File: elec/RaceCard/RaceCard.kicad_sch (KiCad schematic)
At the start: 8 parts

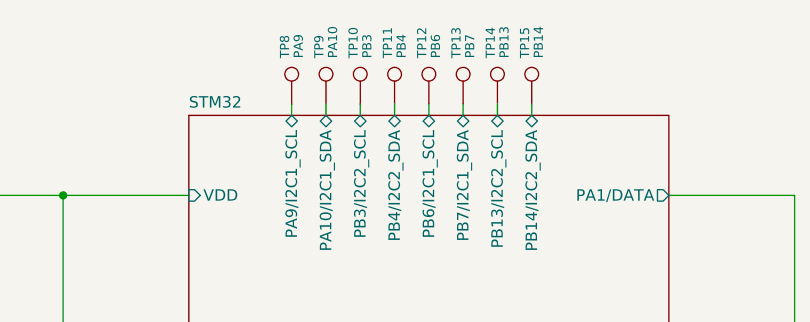
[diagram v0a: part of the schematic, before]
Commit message: Fix des footprints et edge cuts
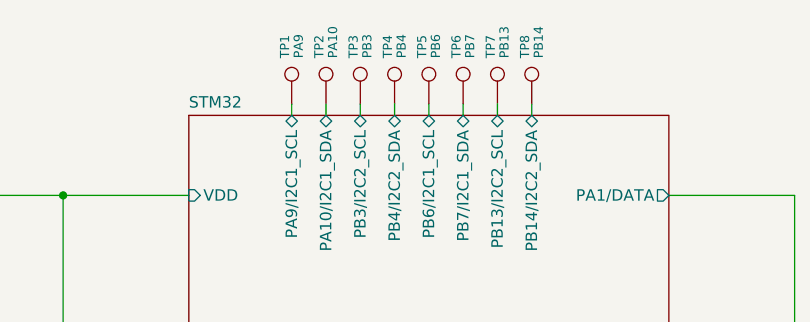
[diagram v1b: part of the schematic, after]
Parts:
- renumbered TP8 to TP1, TP9 to TP2, TP10 to TP3, TP11 to TP4, TP12 to TP5, TP13 to TP6, TP14 to TP7, TP15 to TP8
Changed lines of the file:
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@@
 		(on_board yes)
 		(dnp no)
-		(property "Reference" "TP10"
+		(property "Reference" "TP3"
 			(at 118.618 38.1 90)
 			(effects
@@
 			(project "RaceCard"
 				(path "/fef6ab1d-cc84-41bb-aff7-8da28fd37bf7"
-					(reference "TP10")
+					(reference "TP3")
 					(unit 1)
 				)
@@
 		(on_board yes)
 		(dnp no)
-		(property "Reference" "TP8"
+		(property "Reference" "TP1"
 			(at 110.998 38.1 90)
 			(effects
@@
 			(project ""
 				(path "/fef6ab1d-cc84-41bb-aff7-8da28fd37bf7"
-					(reference "TP8")
+					(reference "TP1")
 					(unit 1)
 				)
@@
 		(on_board yes)
 		(dnp no)
-		(property "Reference" "TP11"
+		(property "Reference" "TP4"
 			(at 122.428 38.1 90)
 			(effects
@@
 			(project "RaceCard"
 				(path "/fef6ab1d-cc84-41bb-aff7-8da28fd37bf7"
-					(reference "TP11")
+					(reference "TP4")
 					(unit 1)
 				)
@@
 		(on_board yes)
 		(dnp no)
-		(property "Reference" "TP14"
+		(property "Reference" "TP7"
 			(at 133.858 38.1 90)
 			(effects
@@
 			(project "RaceCard"
 				(path "/fef6ab1d-cc84-41bb-aff7-8da28fd37bf7"
-					(reference "TP14")
+					(reference "TP7")
 					(unit 1)
 				)
@@
 		(on_board yes)
 		(dnp no)
-		(property "Reference" "TP9"
+		(property "Reference" "TP2"
 			(at 114.808 38.1 90)
 			(effects
@@
 			(project "RaceCard"
 				(path "/fef6ab1d-cc84-41bb-aff7-8da28fd37bf7"
-					(reference "TP9")
+					(reference "TP2")
 					(unit 1)
 				)
@@
 		(on_board yes)
 		(dnp no)
-		(property "Reference" "TP12"
+		(property "Reference" "TP5"
 			(at 126.238 38.1 90)
 			(effects
@@
 			(project "RaceCard"
 				(path "/fef6ab1d-cc84-41bb-aff7-8da28fd37bf7"
-					(reference "TP12")
+					(reference "TP5")
 					(unit 1)
 				)
@@
 		(on_board yes)
 		(dnp no)
-		(property "Reference" "TP13"
+		(property "Reference" "TP6"
 			(at 130.048 38.1 90)
 			(effects
@@
 			(project "RaceCard"
 				(path "/fef6ab1d-cc84-41bb-aff7-8da28fd37bf7"
-					(reference "TP13")
+					(reference "TP6")
 					(unit 1)
 				)
@@
 		(on_board yes)
 		(dnp no)
-		(property "Reference" "TP15"
+		(property "Reference" "TP8"
 			(at 137.668 38.1 90)
 			(effects
@@
 			(project "RaceCard"
 				(path "/fef6ab1d-cc84-41bb-aff7-8da28fd37bf7"
-					(reference "TP15")
-					(unit 1)
-				)
+					(reference "TP8")
+					(unit 1)
+				)

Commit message: Power net update et cleanup sch
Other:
- sheet Power ports: added none; removed GND, VDD
- sheet RF ports: added none; removed GND, VDD
- sheet STM32 ports: added none; removed GND, VDD
- sheet Sensors ports: added none; removed GND, VDD

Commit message: Manque juste RF
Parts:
- added VREGA, VREGD: PB14, TestPoint:TestPoint_Pad_2.0x2.0mm, symbol Connector:TestPoint
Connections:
- net Sensors/VREGA: now also VREGA.1
- net Sensors/VREGD: now also VREGD.1
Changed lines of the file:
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@@
 	(wire
 		(pts
+			(xy 99.06 106.68) (xy 100.33 106.68)
+		)
+		(stroke
+			(width 0)
+			(type default)
+		)
+	)
+	(wire
+		(pts
 			(xy 153.67 74.93) (xy 162.56 74.93)
 		)
@@
 	(wire
 		(pts
+			(xy 99.06 110.49) (xy 100.33 110.49)
+		)
+		(stroke
+			(width 0)
+			(type default)
+		)
+	)
+	(wire
+		(pts
 			(xy 111.76 43.18) (xy 111.76 44.45)
 		)
@@
 	(symbol
 		(lib_id "Connector:TestPoint")
+		(at 99.06 110.49 90)
+		(unit 1)
+		(exclude_from_sim no)
+		(in_bom yes)
+		(on_board yes)
+		(dnp no)
+		(property "Reference" "VREGD"
+			(at 93.98 111.252 90)
+			(effects
+				(font
+					(size 1.016 1.016)
+				)
+				(justify left)
+			)
+		)
+		(property "Value" "PB14"
+			(at 93.98 109.728 90)
+			(effects
+				(font
+					(size 1.016 1.016)
+				)
+				(justify left)
+			)
+		)
+		(property "Footprint" "TestPoint:TestPoint_Pad_2.0x2.0mm"
+			(at 99.06 105.41 0)
+			(effects
+				(font
+					(size 1.27 1.27)
+				)
+				(hide yes)
+			)
+		)
+		(property "Datasheet" "~"
+			(at 99.06 105.41 0)
+			(effects
+				(font
+					(size 1.27 1.27)
+				)
+				(hide yes)
+			)
+		)
+		(property "Description" "test point"
+			(at 99.06 110.49 0)
+			(effects
+				(font
+					(size 1.27 1.27)
+				)
+				(hide yes)
+			)
+		)
+		(pin "1"
+		)
+		(instances
+			(project "RaceCard"
+				(path "/fef6ab1d-cc84-41bb-aff7-8da28fd37bf7"
+					(reference "VREGD")
+					(unit 1)
+				)
+			)
+		)
+	)
+	(symbol
+		(lib_id "Connector:TestPoint")
 		(at 115.57 43.18 0)
 		(unit 1)
@@
 		)
 	)
+	(symbol
+		(lib_id "Connector:TestPoint")
+		(at 99.06 106.68 90)
+		(unit 1)
+		(exclude_from_sim no)
+		(in_bom yes)
+		(on_board yes)
+		(dnp no)
+		(property "Reference" "VREGA"
+			(at 93.98 107.442 90)
+			(effects
+				(font
+					(size 1.016 1.016)
+				)
+				(justify left)
+			)
+		)
+		(property "Value" "PB14"
+			(at 93.98 105.918 90)
+			(effects
+				(font
+					(size 1.016 1.016)
+				)
+				(justify left)
+			)
+		)
+		(property "Footprint" "TestPoint:TestPoint_Pad_2.0x2.0mm"
+			(at 99.06 101.6 0)
+			(effects
+				(font
+					(size 1.27 1.27)
+				)
+				(hide yes)
+			)
+		)
+		(property "Datasheet" "~"
+			(at 99.06 101.6 0)
+			(effects
+				(font
+					(size 1.27 1.27)
+				)
+				(hide yes)
+			)
+		)
+		(property "Description" "test point"
+			(at 99.06 106.68 0)
+			(effects
+				(font
+					(size 1.27 1.27)
+				)
+				(hide yes)
+			)
+		)
+		(pin "1"
+		)
+		(instances
+			(project "RaceCard"
+				(path "/fef6ab1d-cc84-41bb-aff7-8da28fd37bf7"
+					(reference "VREGA")
+					(unit 1)
+				)
+			)
+		)
+	)
 	(sheet
 		(at 100.33 138.43)
@@
 	)
 	(sheet
-		(at 62.23 99.06)
+		(at 62.23 138.43)
 		(size 33.02 31.75)
 		(exclude_from_sim no)
@@
 		)
 		(property "Sheetname" "Power"
-			(at 62.23 98.3484 0)
+			(at 62.23 137.7184 0)
 			(effects
 				(font
@@
 		)
 		(property "Sheetfile" "power.kicad_sch"
-			(at 62.23 131.3946 0)
+			(at 62.23 170.7646 0)
 			(effects
 				(font
@@
 		)
 		(pin "VREGD" output
-			(at 100.33 109.22 180)
+			(at 100.33 110.49 180)
 			(effects
 				(font
